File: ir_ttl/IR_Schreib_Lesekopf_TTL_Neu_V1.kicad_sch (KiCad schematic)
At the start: 18 parts, among them IC1 74LVC1G17DBVR, IC2 74LVC1G17DBVR, T1 SFH309FA-4, T2 BC807-40, T3 BC817-40, X1 +UB, X2 TXD, X3 RXD, X4 GND

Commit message: updated some footprints and cutouts WIP
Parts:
- IC1, IC2: footprint IR_Schreib_Lesekopf_TTL_Neu_V1:SOT23_5 -> Package_TO_SOT_SMD:SOT-23-5; symbol IR_Schreib_Lesekopf_TTL_Neu_V1-eagle-import:74LVC1G17DBVR -> 74xGxx:74LVC1G17
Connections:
- net +UB renamed VDD
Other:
- moved on the sheet: C1, C2, R1, X2, X3, X4

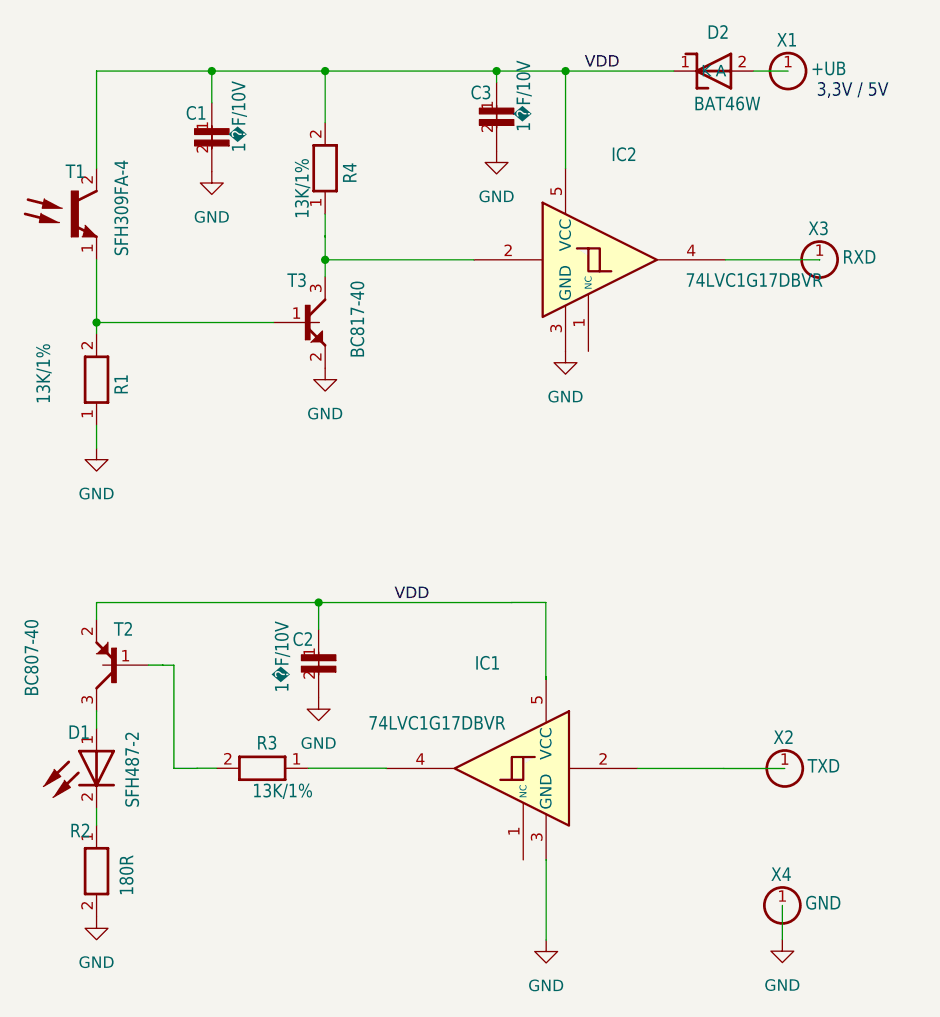
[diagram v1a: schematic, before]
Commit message: ir_ttl passing DRC
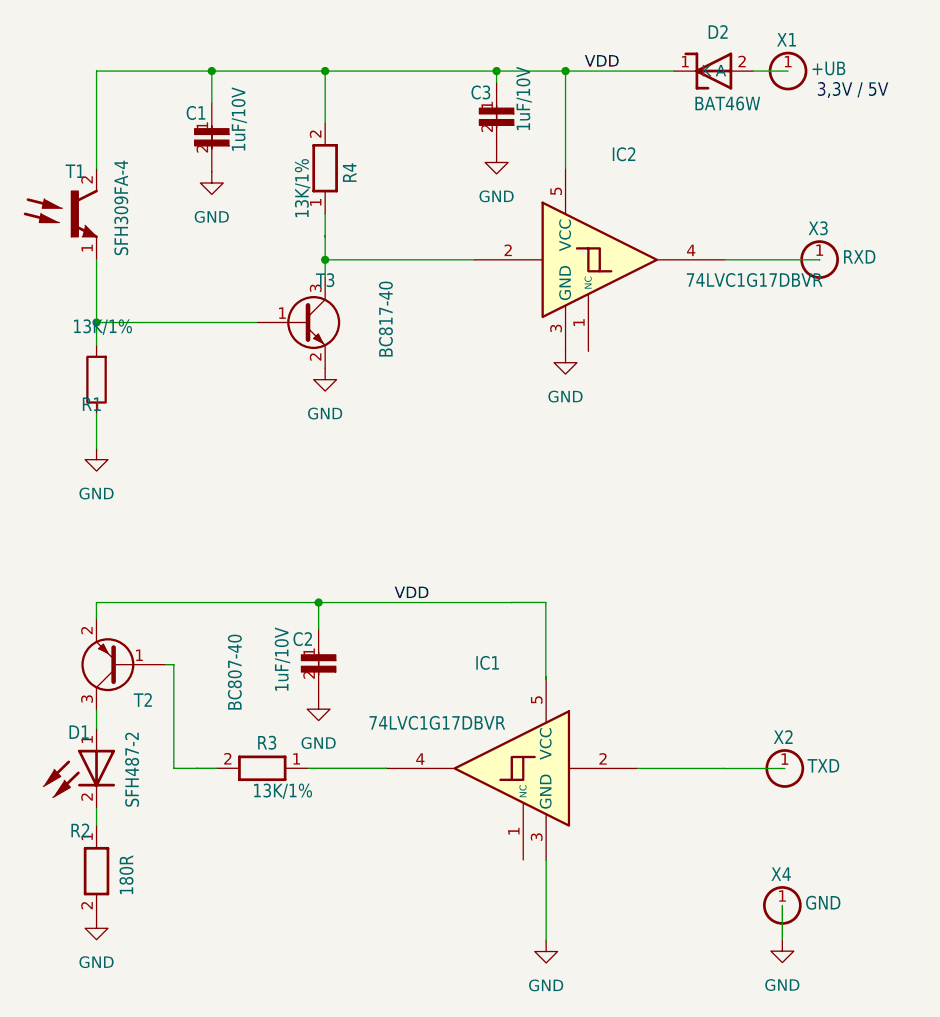
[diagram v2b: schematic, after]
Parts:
- C1, C2, C3: value 1�F/10V -> 1uF/10V
- R1: symbol IR_Schreib_Lesekopf_TTL_Neu_V1-eagle-import:13K/1% -> Device:R
- T2: footprint IR_Schreib_Lesekopf_TTL_Neu_V1:SOT23_3 -> Package_TO_SOT_SMD:SOT-23; symbol IR_Schreib_Lesekopf_TTL_Neu_V1-eagle-import:BC807-40 -> Transistor_BJT:BC807
- T3: footprint IR_Schreib_Lesekopf_TTL_Neu_V1:SOT23_3 -> Package_TO_SOT_SMD:SOT-23; symbol IR_Schreib_Lesekopf_TTL_Neu_V1-eagle-import:BC817-40 -> Transistor_BJT:BC817
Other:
- moved on the sheet: T2
